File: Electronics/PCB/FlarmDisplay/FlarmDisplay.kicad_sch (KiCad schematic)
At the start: 65 parts

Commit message: Started work on NMEA test scripts
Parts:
- BZ1: value (none) -> CMI-9705-0380-SMT-TR; footprint (none) -> FlarmDisplay:CMI-9705-0380-SMT-TR
- C1, C12, C3, C6, C8: value (none) -> 100nF; footprint (none) -> Capacitor_SMD:C_0402_1005Metric
- C10, C11: value (none) -> 10pF; footprint (none) -> Capacitor_SMD:C_0402_1005Metric
- C13, C14, C2, C4: value (none) -> 10nF; footprint (none) -> Capacitor_SMD:C_0402_1005Metric
- C5, C7: value (none) -> 1uF; footprint (none) -> Capacitor_SMD:C_0402_1005Metric
- C9: value (none) -> 4.7uF; footprint (none) -> Capacitor_SMD:C_0805_2012Metric
- D1: value (none) -> PD3S0230-7; footprint (none) -> FlarmDisplay:POWERDI323
- D10: value (none) -> 04Y; footprint (none) -> LED_SMD:LED_0805_2012Metric
- D11: value (none) -> 11Y; footprint (none) -> LED_SMD:LED_0805_2012Metric
- D12: value (none) -> 05Y; footprint (none) -> LED_SMD:LED_0805_2012Metric
- D13: value (none) -> 10Y; footprint (none) -> LED_SMD:LED_0805_2012Metric
- D14: value (none) -> 06Y; footprint (none) -> LED_SMD:LED_0805_2012Metric
- D15: value (none) -> 09Y; footprint (none) -> LED_SMD:LED_0805_2012Metric
- D16: value (none) -> 07Y; footprint (none) -> LED_SMD:LED_0805_2012Metric
- D17: value (none) -> 08Y; footprint (none) -> LED_SMD:LED_0805_2012Metric
- D18: value (none) -> 04R; footprint (none) -> LED_SMD:LED_0805_2012Metric
- D19: value (none) -> GPS; footprint (none) -> LED_SMD:LED_0805_2012Metric
- D2: value (none) -> 12Y; footprint (none) -> LED_SMD:LED_0805_2012Metric
- D20: value (none) -> 05R; footprint (none) -> LED_SMD:LED_0805_2012Metric
- D21: value (none) -> TX; footprint (none) -> LED_SMD:LED_0805_2012Metric
- D22: value (none) -> 06R; footprint (none) -> LED_SMD:LED_0805_2012Metric
- D23: value (none) -> RX; footprint (none) -> LED_SMD:LED_0805_2012Metric
- D24: value (none) -> 07R; footprint (none) -> LED_SMD:LED_0805_2012Metric
- D25: value (none) -> HH; footprint (none) -> LED_SMD:LED_0805_2012Metric
- D26: value (none) -> 08R; footprint (none) -> LED_SMD:LED_0805_2012Metric
- D27: value (none) -> H; footprint (none) -> LED_SMD:LED_0805_2012Metric
- D28: value (none) -> 09R; footprint (none) -> LED_SMD:LED_0805_2012Metric
- D29: value (none) -> M; footprint (none) -> LED_SMD:LED_0805_2012Metric
- D3: value (none) -> 03R; footprint (none) -> LED_SMD:LED_0805_2012Metric
- D30: value (none) -> 10R; footprint (none) -> LED_SMD:LED_0805_2012Metric
- D31: value (none) -> L; footprint (none) -> LED_SMD:LED_0805_2012Metric
- D32: value (none) -> 11R; footprint (none) -> LED_SMD:LED_0805_2012Metric
- D33: value (none) -> LL; footprint (none) -> LED_SMD:LED_0805_2012Metric
- D4: value (none) -> 01Y; footprint (none) -> LED_SMD:LED_0805_2012Metric
- D5: value (none) -> 02R; footprint (none) -> LED_SMD:LED_0805_2012Metric
- D6: value (none) -> 02Y; footprint (none) -> LED_SMD:LED_0805_2012Metric
- D7: value (none) -> 01R; footprint (none) -> LED_SMD:LED_0805_2012Metric
- D8: value (none) -> 03Y; footprint (none) -> LED_SMD:LED_0805_2012Metric
- D9: value (none) -> 12R; footprint (none) -> LED_SMD:LED_0805_2012Metric
- J1: value (none) -> RJ12; footprint (none) -> FlarmDisplay:RJE231660413T
- J2: value (none) -> SWD; footprint (none) -> Connector_PinHeader_2.54mm:PinHeader_1x04_P2.54mm_Vertical
- R1: value (none) -> 200; footprint (none) -> Resistor_SMD:R_0402_1005Metric
- R2: value (none) -> 10K; footprint (none) -> Resistor_SMD:R_0402_1005Metric
- R3, R4: value (none) -> 2K6; footprint (none) -> Resistor_SMD:R_0402_1005Metric
- SW1: value (none) -> RESET; footprint (none) -> FlarmDisplay:SMT_J
- SW2: value (none) -> BOOT; footprint (none) -> FlarmDisplay:7814G-1-023E
- TP1: value (none) -> 3.3V; footprint (none) -> TestPoint:TestPoint_Pad_D2.0mm
- TP2: value (none) -> GND; footprint (none) -> TestPoint:TestPoint_Pad_D2.0mm
- TP3: value (none) -> USART2_TX; footprint (none) -> TestPoint:TestPoint_Pad_D2.0mm
- TP4: value (none) -> USART2_RX; footprint (none) -> TestPoint:TestPoint_Pad_D2.0mm
- U1: value (none) -> IPN80R3K3P7ATMA1; footprint (none) -> Package_TO_SOT_SMD:SOT-223-3_TabPin2
- U2: value (none) -> STM32F334K8Ux; footprint (none) -> Package_DFN_QFN:QFN-32-1EP_5x5mm_P0.5mm_EP3.45x3.45mm
- U3, U4: value (none) -> TLC5928; footprint (none) -> Package_DFN_QFN:VQFN-24-1EP_4x4mm_P0.5mm_EP2.45x2.45mm
- Y1: value (none) -> 16MHz; footprint (none) -> Crystal:Crystal_SMD_3225-4Pin_3.2x2.5mm
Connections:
- no-connect marks 15 -> 14

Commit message: Updated PCB to v0.2
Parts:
- removed SW2: BOOT, FlarmDisplay:7814G-1-023E, symbol Switch:SW_SPDT
- added JP1: BOOT, Jumper:SolderJumper-3_P1.3mm_Open_RoundedPad1.0x1.5mm, symbol Jumper:SolderJumper_3_Open
- added U5: MAX318xE, Package_TO_SOT_SMD:SOT-23-5, symbol FlarmDisplay:MAX318xE
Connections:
- net +3V3: now also JP1.3 (B), U5.5 (VCC)
- net GND: now also JP1.1 (A), U5.1 (~{EN}), U5.2 (GND)
- net RX: now also U5.3 (ROUT); no longer J1.3
- net at R2.2: now also JP1.2 (C)
- net TX: no longer names the net of U2.19 (PA9)
- net TX: no longer J1.2
- new net: J1.3, U5.4 (RIN)
- no-connect marks 14 -> 15
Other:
- moved on the sheet: J1, J2

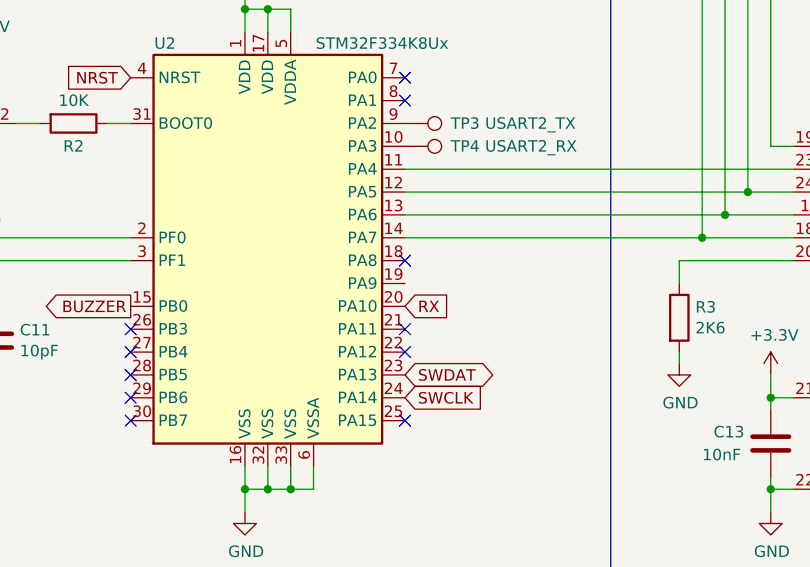
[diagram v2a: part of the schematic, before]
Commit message: Basic firmware LED test working
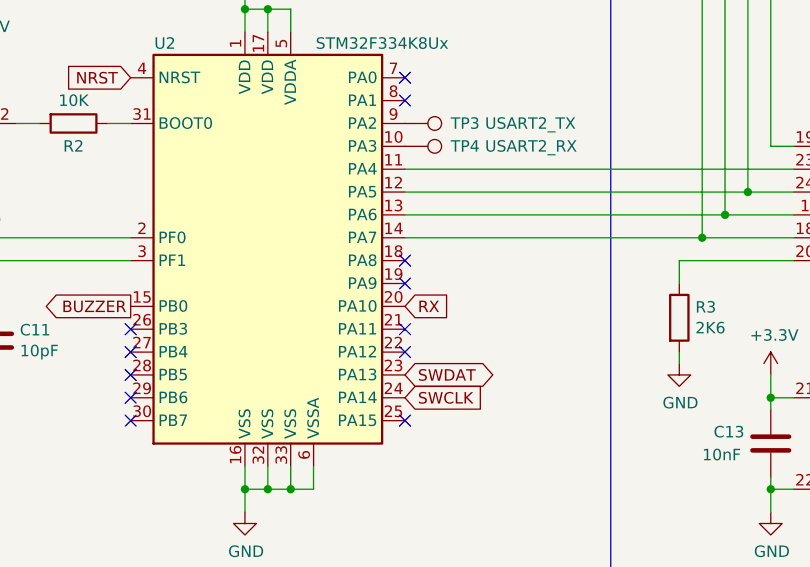
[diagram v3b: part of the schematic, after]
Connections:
- no-connect marks 15 -> 16
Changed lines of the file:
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@@
   (no_connect (at 156.21 48.26))
   (no_connect (at 125.73 83.82))
+  (no_connect (at 156.21 71.12))
   (no_connect (at 156.21 76.2))
   (no_connect (at 125.73 78.74))
